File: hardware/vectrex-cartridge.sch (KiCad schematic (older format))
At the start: 14 parts, among them CON1 vectrex-edge-connector, U1 AT27C256R-70PU / AT27C512R-70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, U2 DS2431+ TO-92

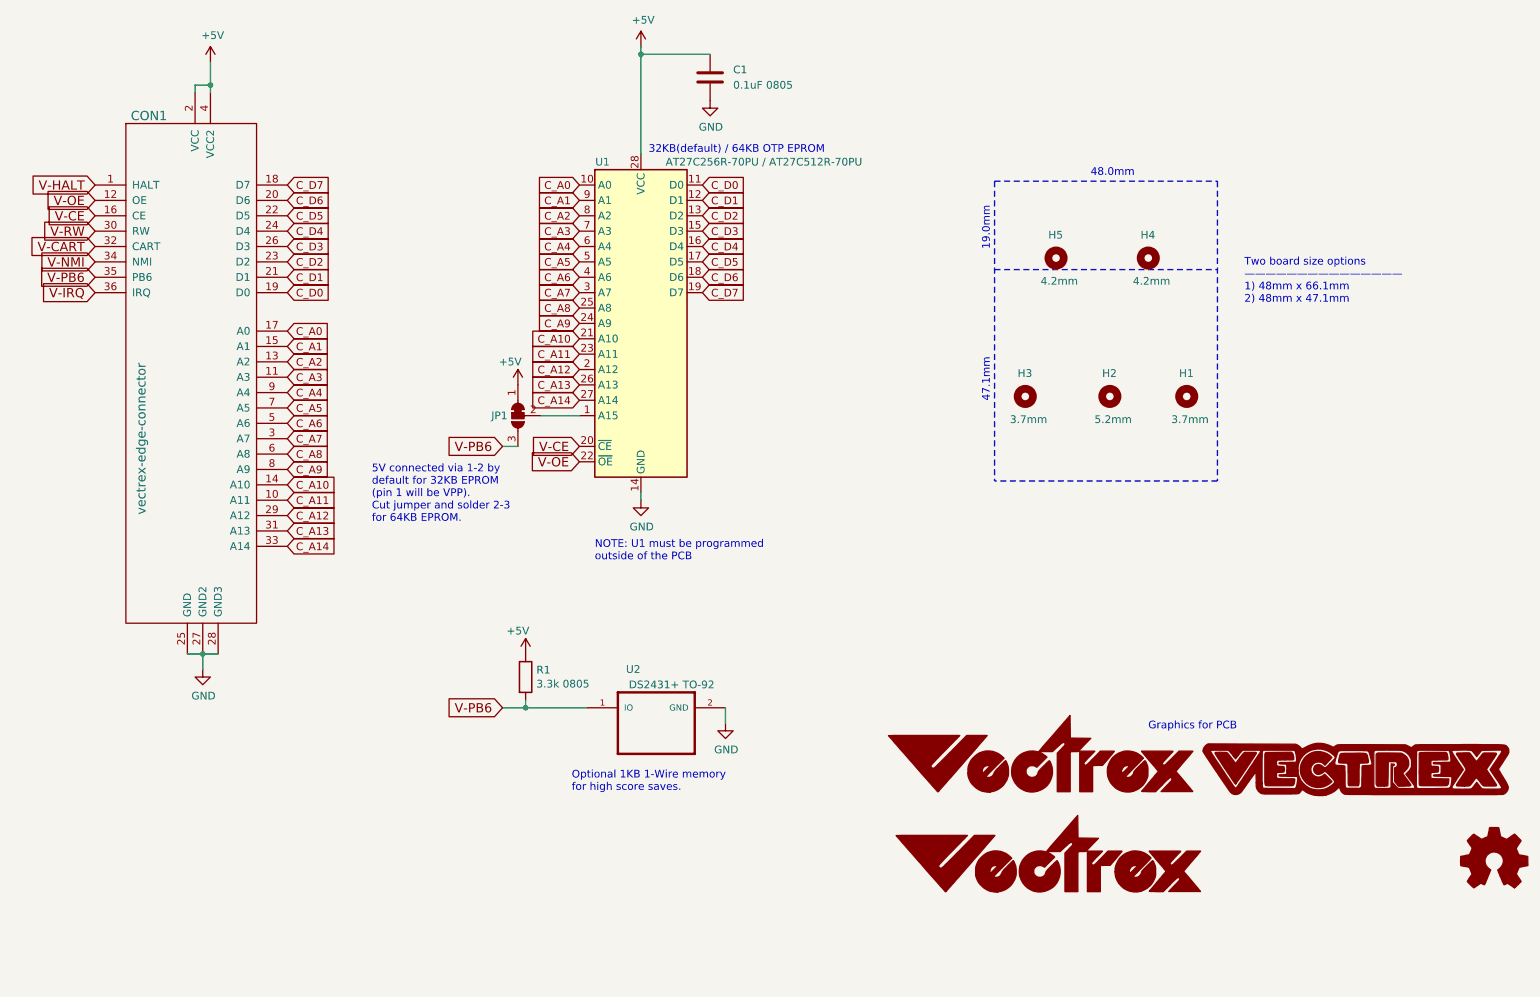
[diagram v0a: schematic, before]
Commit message: added RGB LED to Vectrex Cartridge v1.1, also added stand-alone LED PCB v1.0
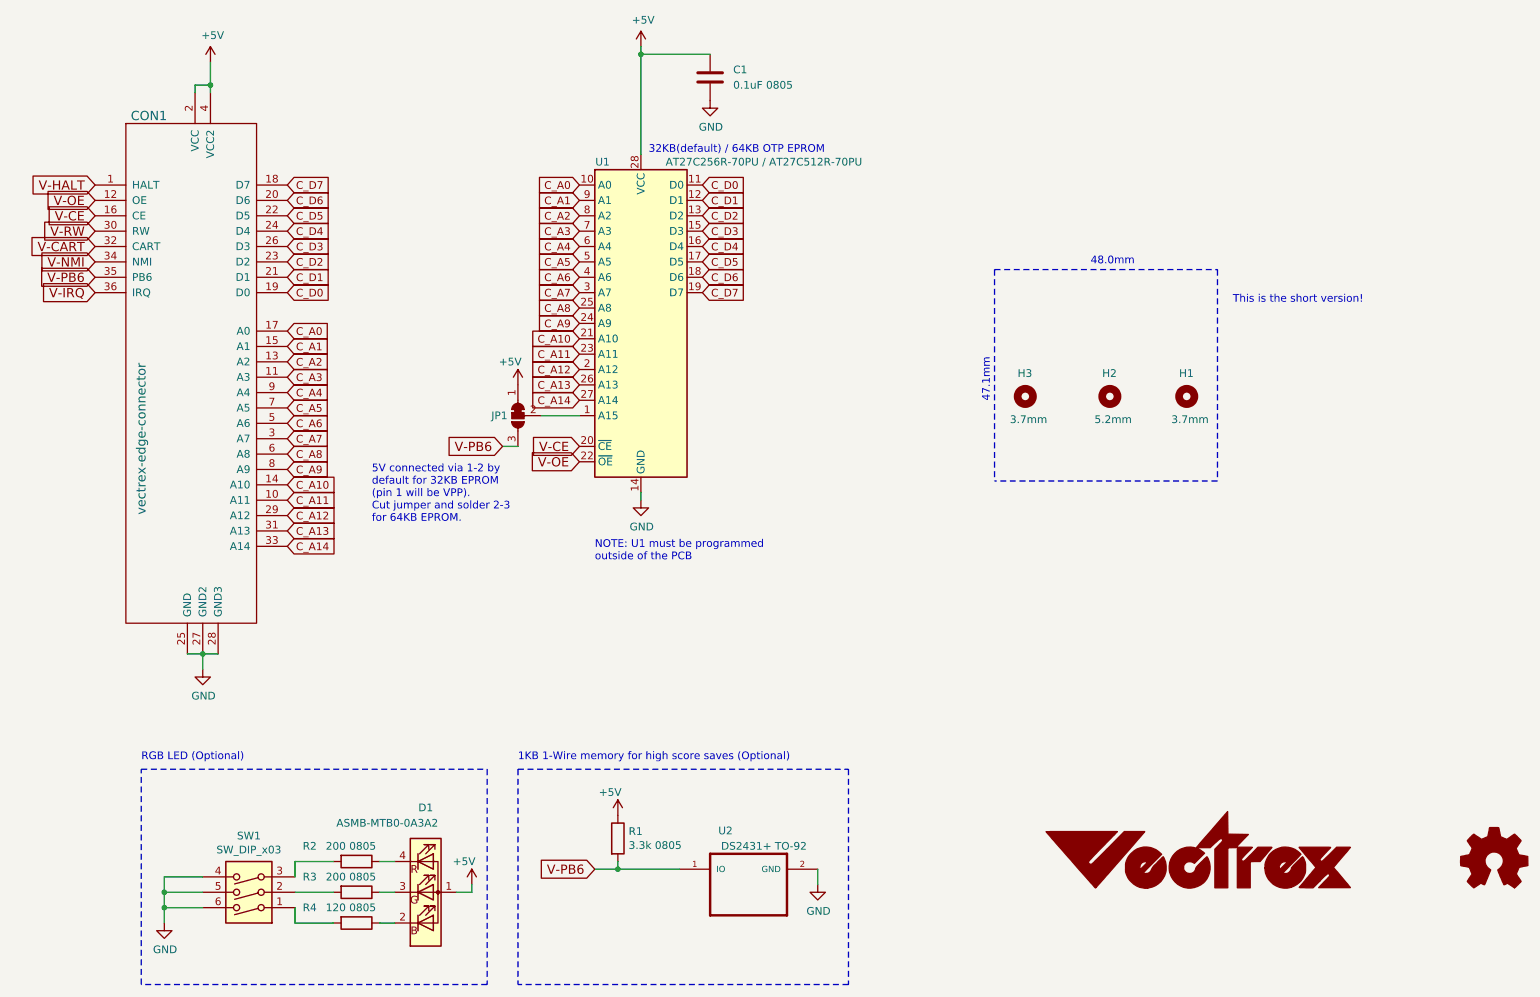
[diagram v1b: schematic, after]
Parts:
- removed G2: LOGO, vectrex-cartridge:vectrex-us-soldermask, symbol vectrex-us:LOGO
- removed G3: LOGO, vectrex-cartridge:vectrex-uk-soldermask, symbol vectrex-uk:LOGO
- removed H4, H5: 4.2mm, vectrex-cartridge:Mounting_Hole_D4.2mm, symbol Mechanical:MountingHole
- added D1: ASMB-MTB0-0A3A2, vectrex-cartridge:LED_Avago_PLCC4_3.2x2.8mm_CW, symbol LED:ASMB-MTB0-0A3A2
- added R2, R3: 200 0805, Resistor_SMD:R_0805_2012Metric_Pad1.15x1.40mm_HandSolder, symbol Device:R
- added R4: 120 0805, Resistor_SMD:R_0805_2012Metric_Pad1.15x1.40mm_HandSolder, symbol Device:R
- added SW1: SW_DIP_x03, Button_Switch_SMD:SW_DIP_SPSTx03_Slide_6.7x9.18mm_W8.61mm_P2.54mm_LowProfile, symbol Switch:SW_DIP_x03
- G1: footprint vectrex-cartridge:vectrex-us-soldermask -> vectrex-cartridge:vectrex-us-soldermask-15mm
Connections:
- net +5V: now also D1.1 (A)
- net GND: now also SW1.4, SW1.5, SW1.6
- new net: D1.2 (BK), R4.1
- new net: D1.3 (GK), R3.1
- new net: D1.4 (RK), R2.1
- new net: R2.2, SW1.3
- new net: R3.2, SW1.2
- new net: R4.2, SW1.1
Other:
- note added: "1KB 1-Wire memory for high score saves (Optional)"
- note added: "RGB LED (Optional)"
- note added: "This is the short version!"
- note removed: "19.0mm\n"
- note removed: "Graphics for PCB"
- note removed: "Optional 1KB 1-Wire memory\nfor high score saves."
- note removed: "Two board size options\n———————————————\n1) 48mm x 66.1mm\n2) 48mm x 47.1mm"
- moved on the sheet: R1, U2
